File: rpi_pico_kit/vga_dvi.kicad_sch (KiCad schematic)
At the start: 32 parts, among them J4 DB15_Female_HighDensity_Mount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, J5 HDMI_A

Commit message: added MPNs
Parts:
- J4, JP10, JP11, JP12, JP13, JP14, JP3, JP6, JP7, JP8, JP9: Supplier (none) -> me
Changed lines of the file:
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@@
+      (effects (font (size 1.27 1.27)) hide)
+    )
+    (property "Supplier" "me" (id 5) (at 140.97 90.17 0)
       (effects (font (size 1.27 1.27)) hide)
     )
@@
     )
     (property "Datasheet" "~" (id 3) (at 88.9 80.01 0)
+      (effects (font (size 1.27 1.27)) hide)
+    )
+    (property "Supplier" "me" (id 4) (at 113.03 90.17 0)
       (effects (font (size 1.27 1.27)) hide)
     )
@@
       (effects (font (size 1.27 1.27)) hide)
     )
+    (property "Supplier" "me" (id 5) (at 41.91 115.57 0)
+      (effects (font (size 1.27 1.27)) hide)
+    )
     (pin "1")
     (pin "2")
@@
     )
     (property "Manufacturer Part Number" "PinHeader_1x02" (id 4) (at 41.91 95.25 0)
+      (effects (font (size 1.27 1.27)) hide)
+    )
+    (property "Supplier" "me" (id 5) (at 41.91 95.25 0)
       (effects (font (size 1.27 1.27)) hide)
     )
@@
       (effects (font (size 1.27 1.27)) hide)
     )
+    (property "Supplier" "me" (id 5) (at 41.91 100.33 0)
+      (effects (font (size 1.27 1.27)) hide)
+    )
     (pin "1")
     (pin "2")
@@
       (effects (font (size 1.27 1.27)) hide)
     )
+    (property "Supplier" "me" (id 5) (at 41.91 80.01 0)
+      (effects (font (size 1.27 1.27)) hide)
+    )
     (pin "1")
     (pin "2")
@@
     )
     (property "Manufacturer Part Number" "PinHeader_1x02" (id 4) (at 41.91 69.85 0)
+      (effects (font (size 1.27 1.27)) hide)
+    )
+    (property "Supplier" "me" (id 5) (at 41.91 69.85 0)
       (effects (font (size 1.27 1.27)) hide)
     )
@@
       (effects (font (size 1.27 1.27)) hide)
     )
+    (property "Supplier" "me" (id 5) (at 140.97 95.25 0)
+      (effects (font (size 1.27 1.27)) hide)
+    )
     (pin "1")
     (pin "2")
@@
       (effects (font (size 1.27 1.27)) hide)
     )
+    (property "Supplier" "me" (id 5) (at 41.91 74.93 0)
+      (effects (font (size 1.27 1.27)) hide)
+    )
     (pin "1")
     (pin "2")
@@
       (effects (font (size 1.27 1.27)) hide)
     )
+    (property "Supplier" "me" (id 5) (at 41.91 110.49 0)
+      (effects (font (size 1.27 1.27)) hide)
+    )
     (pin "1")
     (pin "2")
@@
       (effects (font (size 1.27 1.27)) hide)
     )
+    (property "Supplier" "me" (id 5) (at 41.91 90.17 0)
+      (effects (font (size 1.27 1.27)) hide)
+    )

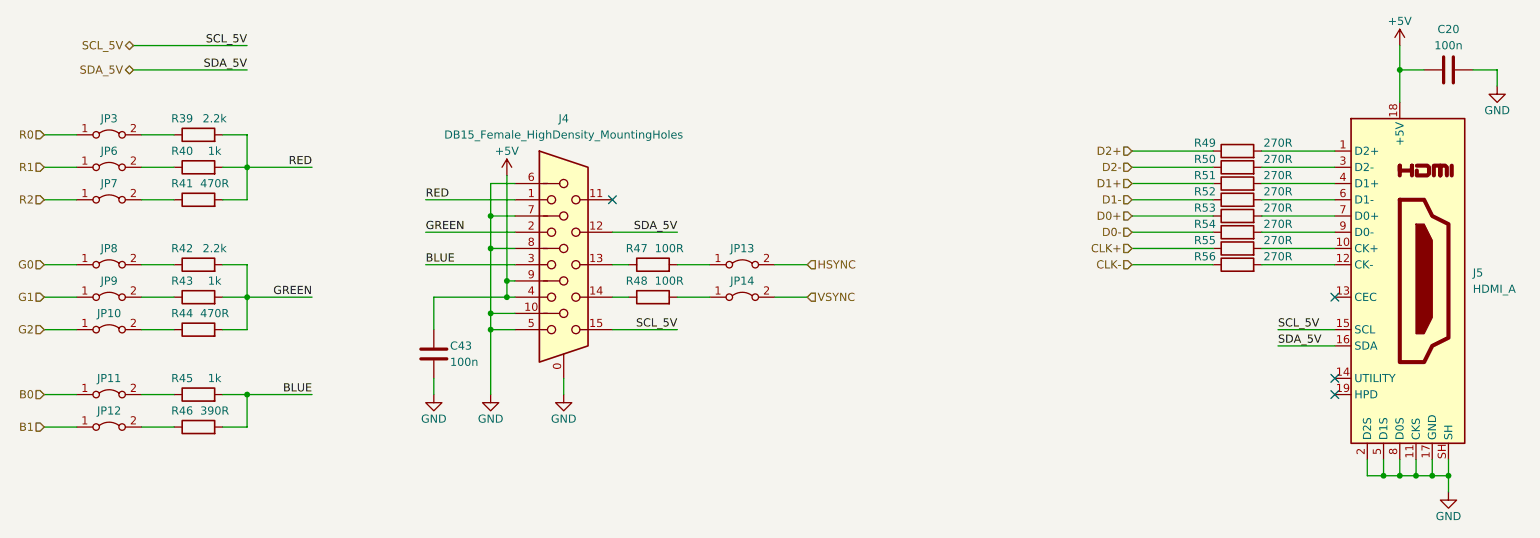
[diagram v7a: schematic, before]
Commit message: changed numbering of parts
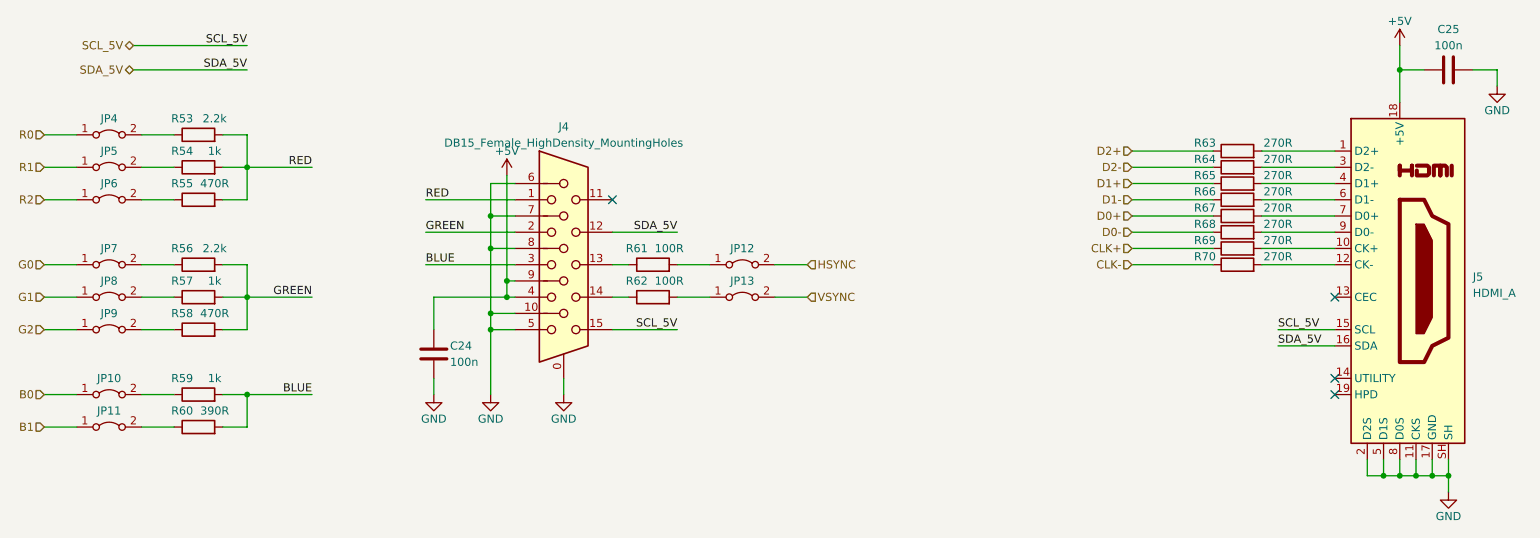
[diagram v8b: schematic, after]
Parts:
- renumbered C43 to C24, C20 to C25, JP11 to JP10, JP12 to JP11, JP13 to JP12, JP14 to JP13, JP3 to JP4, JP6 to JP5, JP7 to JP6, JP8 to JP7, JP9 to JP8, JP10 to JP9, R39 to R53, R40 to R54, R41 to R55, R42 to R56, R43 to R57, R44 to R58, R45 to R59, R46 to R60, R47 to R61, R48 to R62, R49 to R63, R50 to R64, R51 to R65, R52 to R66, R53 to R67, R54 to R68, R55 to R69, R56 to R70
